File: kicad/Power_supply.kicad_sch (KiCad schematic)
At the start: 17 parts, among them U3 AP3211K, U4 AP3211K

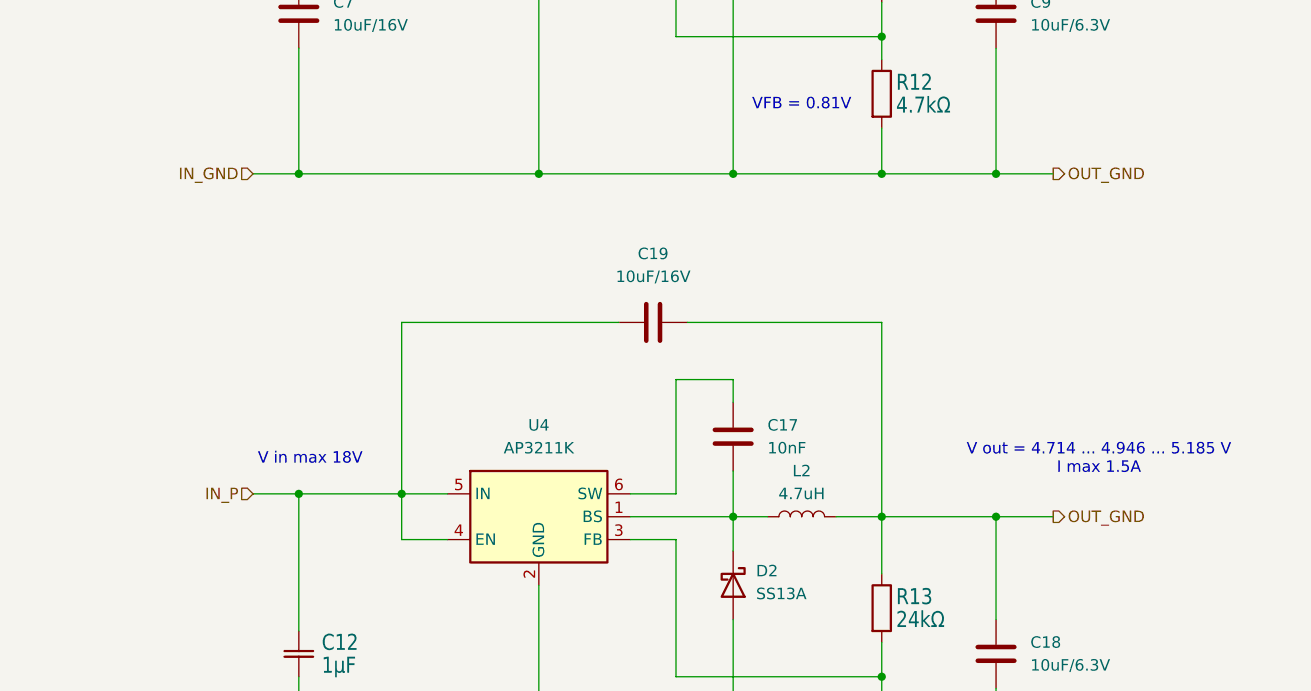
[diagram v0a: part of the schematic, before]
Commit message: Update project. Route signals, make a coplanar 50 R output - two layer board.
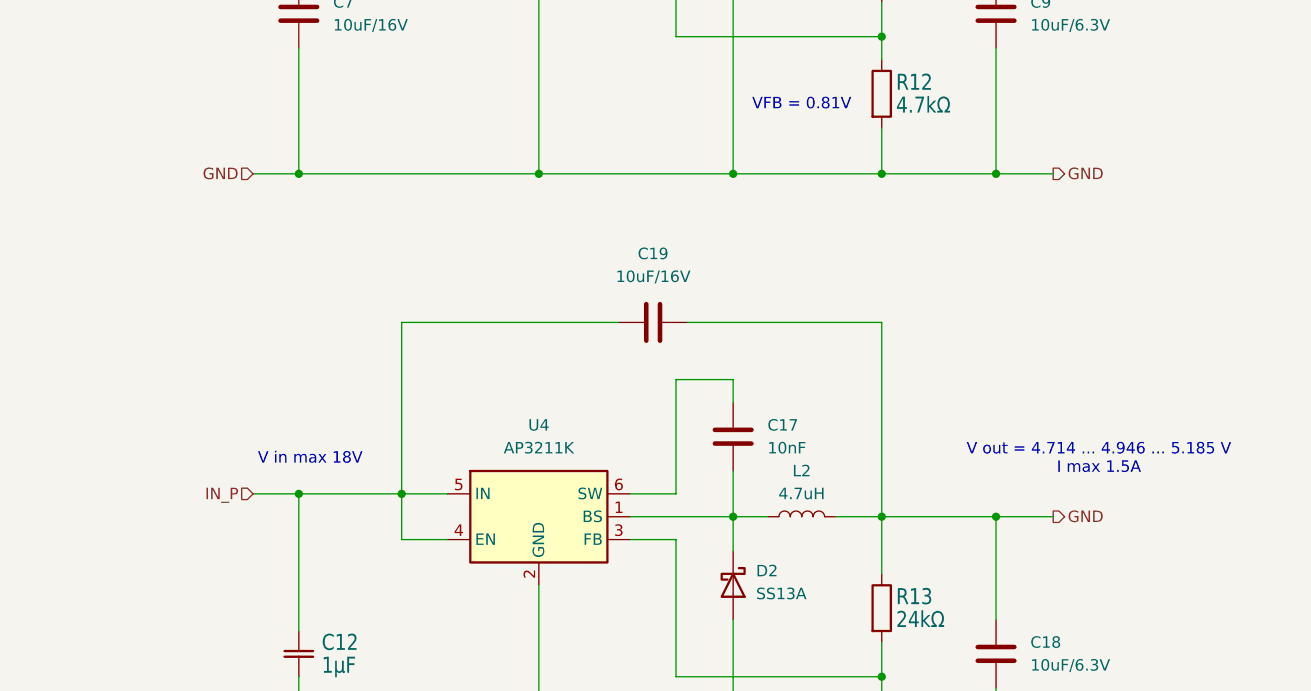
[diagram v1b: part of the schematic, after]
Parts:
- D1, D2: footprint Diode_SMD:D_SMA -> Diode_SMD:D_SMB
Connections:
- net IN_GND renamed GND
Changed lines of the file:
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@@
 		)
 	)
-	(hierarchical_label "OUT_GND"
+	(hierarchical_label "GND"
 		(shape output)
 		(at 190.5 111.76 0)
@@
 		)
 	)
-	(hierarchical_label "OUT_GND"
+	(hierarchical_label "GND"
 		(shape output)
 		(at 190.5 73.66 0)
@@
 		)
 	)
-	(hierarchical_label "IN_GND"
+	(hierarchical_label "GND"
 		(shape input)
 		(at 101.6 73.66 180)
@@
 			)
 		)
-		(property "Footprint" "Diode_SMD:D_SMA"
+		(property "Footprint" "Diode_SMD:D_SMB"
 			(at 150.495 119.38 0)
 			(effects
@@
 			)
 		)
-		(property "Datasheet" "https://www.tme.eu/Document/f86dbf25808a64c8f6899aa01bdfadcb/SS12A_SER.pdf"
+		(property "Datasheet" "http://www.jameco.com/Jameco/Products/ProdDS/1538777.pdf"
 			(at 154.94 119.38 0)
 			(effects
@@
 			)
 		)
-		(property "Description" "30V 1A Schottky Barrier Rectifier Diode, SMB"
+		(property "Description" "40V 2A Schottky Barrier Rectifier Diode, SMB"
 			(at 154.94 119.38 0)
 			(effects
@@
 			)
 		)
-		(property "Datasheet" "https://www.tme.eu/Document/a05ae3504cfc60ed89e3a57fb94acf5e/VIKING-NL.pdf"
+		(property "Datasheet" "~"
 			(at 162.56 40.64 0)
 			(effects
@@
 			)
 		)
-		(property "Description" "Inductor, NL05KTC4R7"
+		(property "Description" "Inductor"
 			(at 162.56 40.64 0)
 			(effects
@@
 			)
 		)
-		(property "Datasheet" "https://www.tme.eu/Document/a05ae3504cfc60ed89e3a57fb94acf5e/VIKING-NL.pdf"
+		(property "Datasheet" "~"
 			(at 162.56 111.76 0)
 			(effects
@@
 			)
 		)
-		(property "Description" "Inductor, NL05KTC4R7"
+		(property "Description" "Inductor"
 			(at 162.56 111.76 0)
 			(effects
@@
 			)
 		)
-		(property "Footprint" "Diode_SMD:D_SMA"
+		(property "Footprint" "Diode_SMD:D_SMB"
 			(at 150.495 48.26 0)
 			(effects
@@
 			)
 		)
-		(property "Datasheet" "https://www.tme.eu/Document/f86dbf25808a64c8f6899aa01bdfadcb/SS12A_SER.pdf"
+		(property "Datasheet" "http://www.jameco.com/Jameco/Products/ProdDS/1538777.pdf"
 			(at 154.94 48.26 0)
 			(effects
@@
 			)
 		)
-		(property "Description" "30V 1A Schottky Barrier Rectifier Diode, SMB"
+		(property "Description" "40V 2A Schottky Barrier Rectifier Diode, SMB"
 			(at 154.94 48.26 0)
 			(effects

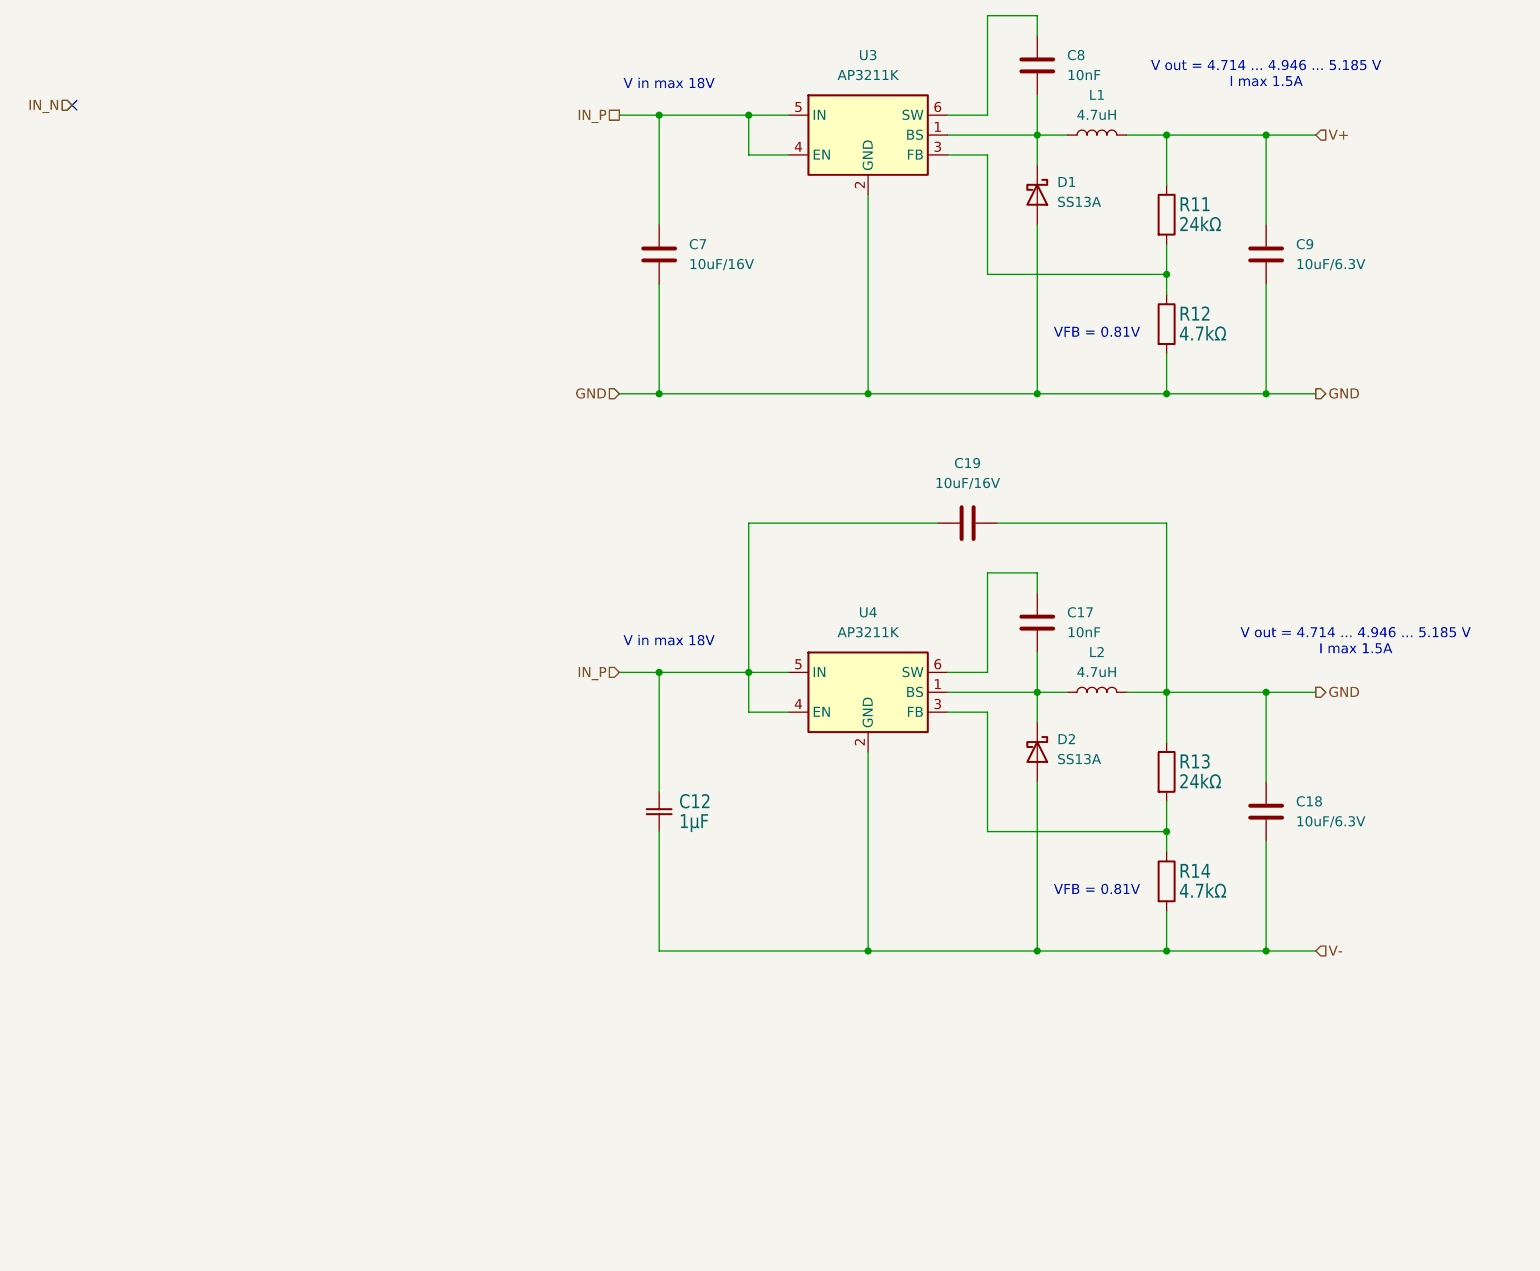
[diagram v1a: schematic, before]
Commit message: 1. Update project regarding to the clean up the rules for the https://jlcpcb.com/ 2. Make the output as Co-planar Wave-guide 50 Ohm 3. Trim the differential input length, and width
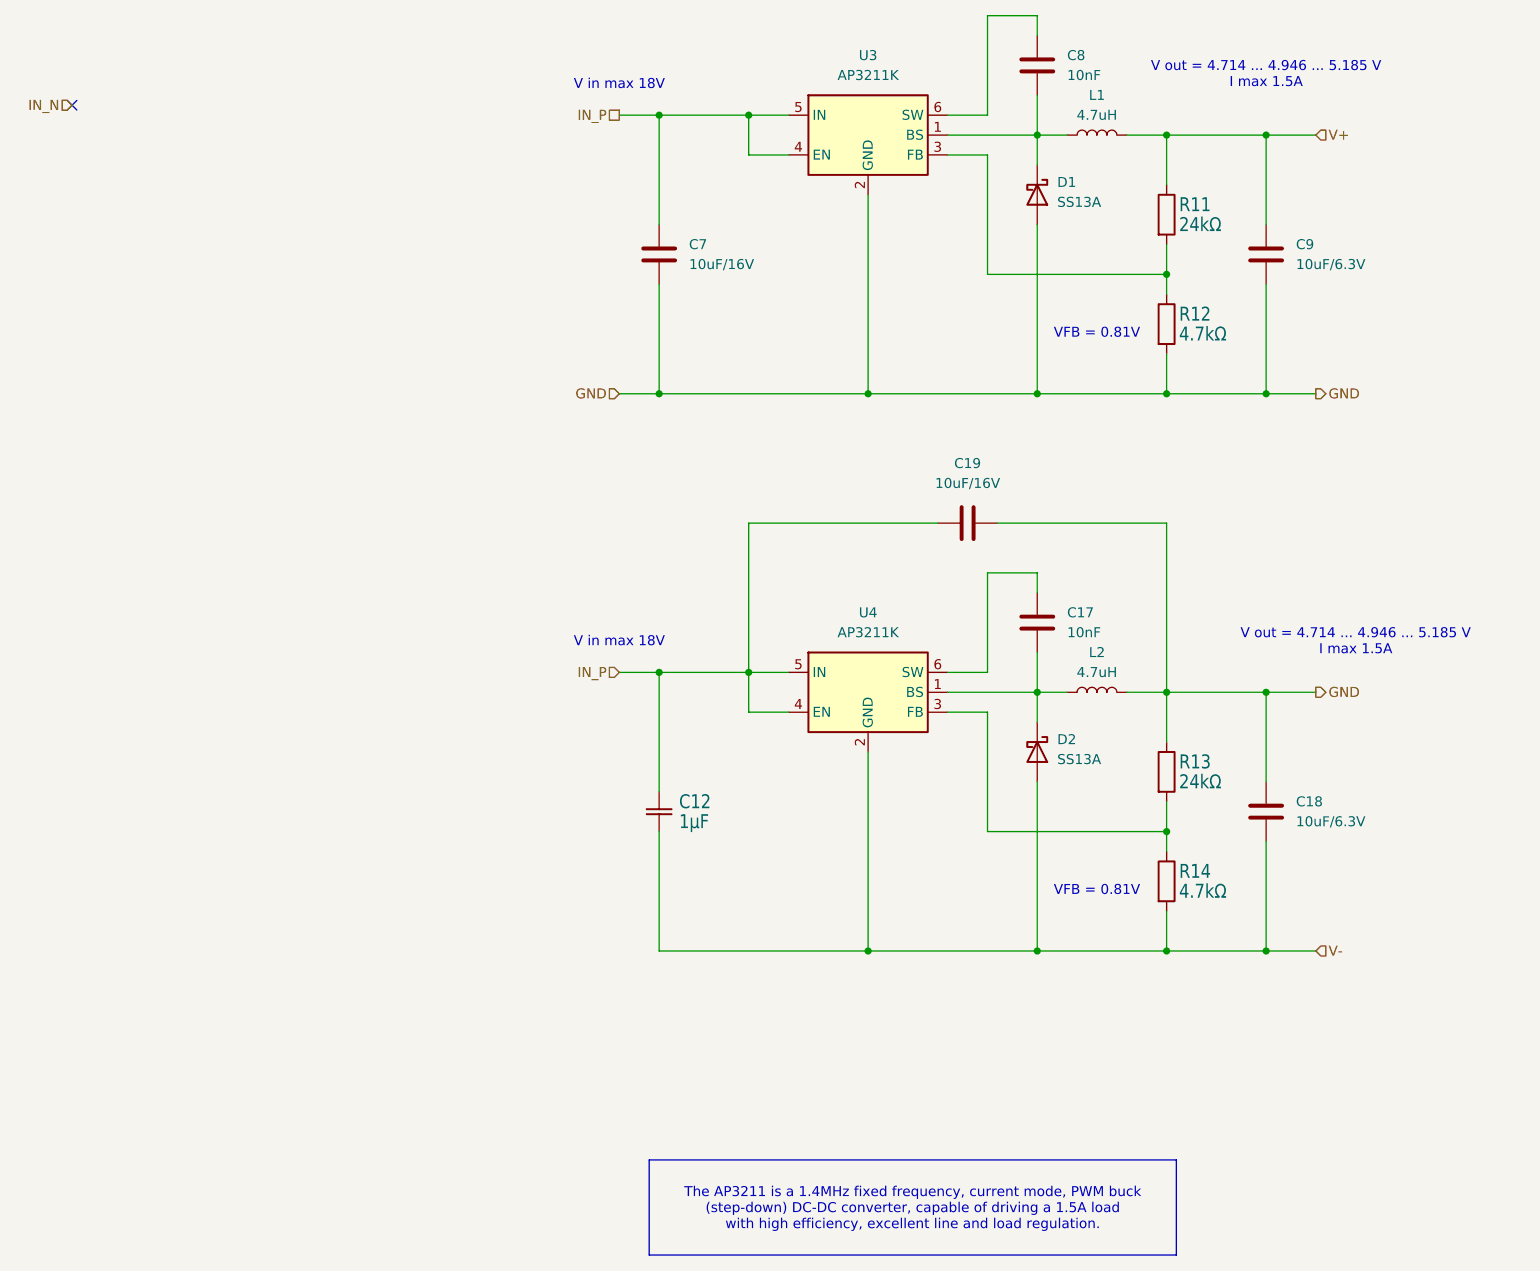
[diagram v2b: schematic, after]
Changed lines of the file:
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@@
 	(text "V in max 18V"
 		(exclude_from_sim no)
-		(at 107.95 105.41 0)
+		(at 101.6 105.41 0)
 		(effects
 			(font
@@
 	(text "V in max 18V"
 		(exclude_from_sim no)
-		(at 107.95 34.29 0)
+		(at 101.6 34.29 0)
 		(effects
 			(font
@@
 			)
 		)
+	)
+	(text_box "The AP3211 is a 1.4MHz fixed frequency, current mode, PWM buck (step-down) DC-DC converter, capable of driving a 1.5A load with high efficiency, excellent line and load regulation. "
+		(exclude_from_sim no)
+		(at 105.41 171.45 0)
+		(size 67.2841 12.1341)
+		(margins 0.9525 0.9525 0.9525 0.9525)
+		(stroke
+			(width 0)
+			(type solid)
+		)
+		(fill
+			(type none)
+		)
+		(effects
+			(font
+				(size 1.27 1.27)
+				(thickness 0.1588)
+			)
+		)
